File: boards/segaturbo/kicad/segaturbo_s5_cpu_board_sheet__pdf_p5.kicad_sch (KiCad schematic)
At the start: 40 parts, among them CN4 Conn_01x06, CN5 Conn_01x12, CN6 Conn_01x06, CN8 Conn_01x46, IC125 74LS259, IC126 75468, IC127 74LS244, IC17 74LS191, IC35b 74LS74, IC5 74LS191, IC6 8255, IC82 74LS48, IC83 74LS48, IC84 8279, IC95 75468, IC96 75468, IC97 74LS145, IC98 74LS145, SW1 DIP_SW_8, SW2 DIP_SW_8

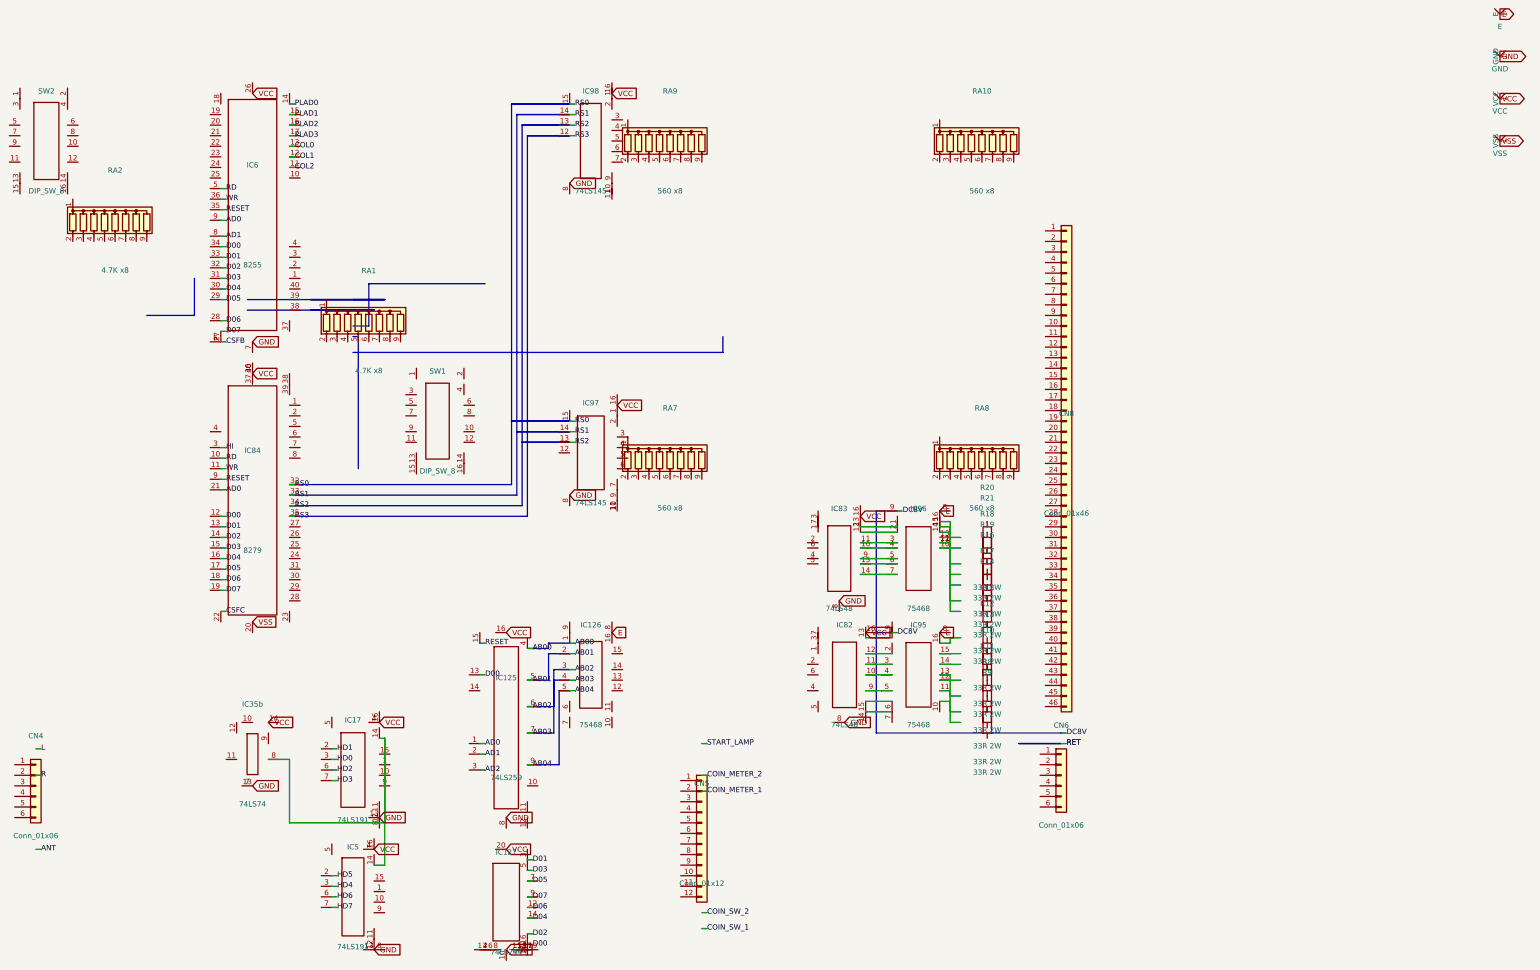
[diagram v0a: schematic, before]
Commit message: Fix KiCad pin-aligned generated symbols
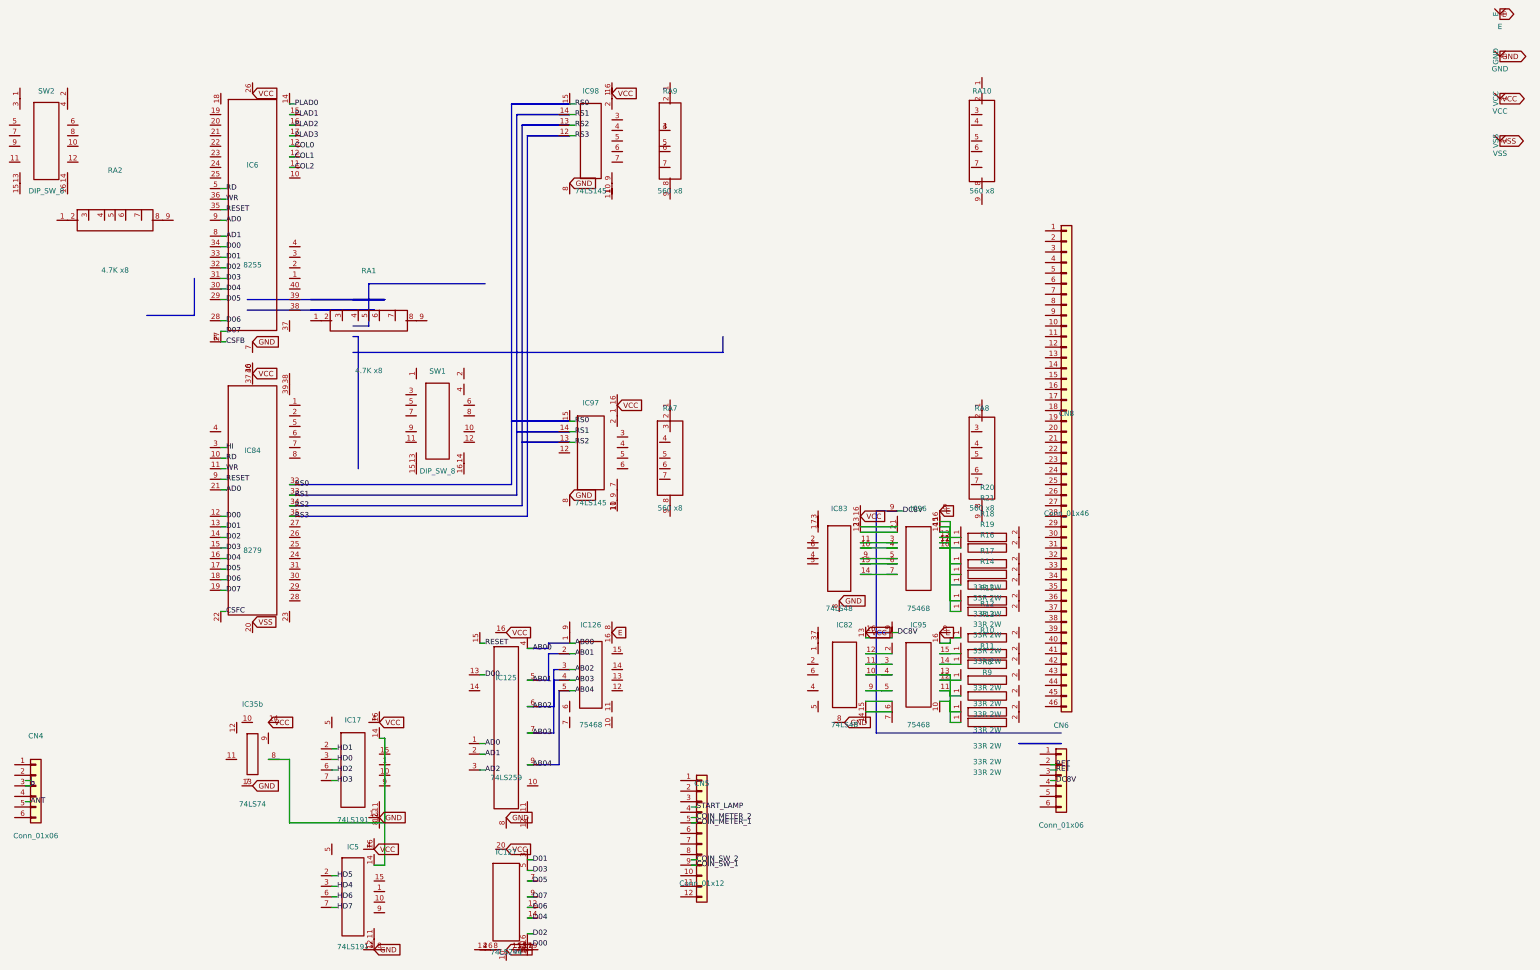
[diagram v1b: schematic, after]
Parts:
- R10: symbol Device:R -> user:_chip_R10
- R11: symbol Device:R -> user:_chip_R11
- R12: symbol Device:R -> user:_chip_R12
- R13: symbol Device:R -> user:_chip_R13
- R14: symbol Device:R -> user:_chip_R14
- R15: symbol Device:R -> user:_chip_R15
- R16: symbol Device:R -> user:_chip_R16
- R17: symbol Device:R -> user:_chip_R17
- R18: symbol Device:R -> user:_chip_R18
- R19: symbol Device:R -> user:_chip_R19
- R20: symbol Device:R -> user:_chip_R20
- R21: symbol Device:R -> user:_chip_R21
- R8: symbol Device:R -> user:_chip_R8
- R9: symbol Device:R -> user:_chip_R9
- RA1: symbol Device:R_Network08 -> user:_chip_RA1
- RA10: symbol Device:R_Network08 -> user:_chip_RA10
- RA2: symbol Device:R_Network08 -> user:_chip_RA2
- RA7: symbol Device:R_Network08 -> user:_chip_RA7
- RA8: symbol Device:R_Network08 -> user:_chip_RA8
- RA9: symbol Device:R_Network08 -> user:_chip_RA9
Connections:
- net at R19.1: now also IC96.10 (7C), IC96.11 (6C), IC96.12 (5C), IC96.13 (4C), IC96.14 (3C), IC96.15 (2C), IC96.16 (1C), R14.1, R16.1, R17.1, R18.1, R20.1, R21.1
- net at R10.1: now also IC95.10 (7C), IC95.11 (6C), IC95.12 (5C), IC95.13 (4C), R11.1, R8.1, R9.1
- net at R10.2: no longer R8.1
- net at RA9.3: now also RA9.4
- net at R13.2: no longer R11.1
- net at R13.1: now also IC95.14 (3C)
- net at R15.1: now also IC95.16 (1C)
- net at R12.1: now also IC95.15 (2C)
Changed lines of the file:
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@@
   )
   (symbol
-    (lib_id "Device:R_Network08")
+    (lib_id "user:_chip_RA2")
     (at 67.31 67.31 0)
     (unit 1)
@@
   )
   (symbol
-    (lib_id "Device:R_Network08")
+    (lib_id "user:_chip_RA1")
     (at 128.27 91.44 0)
     (unit 1)
@@
   )
   (symbol
-    (lib_id "Device:R_Network08")
+    (lib_id "user:_chip_RA9")
     (at 200.66 48.26 0)
     (unit 1)
@@
   )
   (symbol
-    (lib_id "Device:R_Network08")
+    (lib_id "user:_chip_RA10")
     (at 275.59 48.26 0)
     (unit 1)
@@
   )
   (symbol
-    (lib_id "Device:R_Network08")
+    (lib_id "user:_chip_RA7")
     (at 200.66 124.46 0)
     (unit 1)
@@
   )
   (symbol
-    (lib_id "Device:R_Network08")
+    (lib_id "user:_chip_RA8")
     (at 275.59 124.46 0)
     (unit 1)
@@
   )
   (symbol
-    (lib_id "Device:R")
+    (lib_id "user:_chip_R20")
     (at 276.86 143.51 0)
     (unit 1)
@@
   )
   (symbol
-    (lib_id "Device:R")
+    (lib_id "user:_chip_R21")
     (at 276.86 146.05 0)
     (unit 1)
@@
   )
   (symbol
-    (lib_id "Device:R")
+    (lib_id "user:_chip_R18")
     (at 276.86 149.86 0)
     (unit 1)
@@
   )
   (symbol
-    (lib_id "Device:R")
+    (lib_id "user:_chip_R19")
     (at 276.86 152.4 0)
     (unit 1)
@@
   )
   (symbol
-    (lib_id "Device:R")
+    (lib_id "user:_chip_R16")
     (at 276.86 154.94 0)
     (unit 1)
@@
   )
   (symbol
-    (lib_id "Device:R")
+    (lib_id "user:_chip_R17")
     (at 276.86 158.75 0)
     (unit 1)
@@
   )
   (symbol
-    (lib_id "Device:R")
+    (lib_id "user:_chip_R14")
     (at 276.86 161.29 0)
     (unit 1)
@@
   )
   (symbol
-    (lib_id "Device:R")
+    (lib_id "user:_chip_R15")
     (at 276.86 167.64 0)
     (unit 1)
@@
   )
   (symbol
-    (lib_id "Device:R")
+    (lib_id "user:_chip_R12")
     (at 276.86 171.45 0)
     (unit 1)
@@
   )
   (symbol
-    (lib_id "Device:R")
+    (lib_id "user:_chip_R13")
     (at 276.86 173.99 0)
     (unit 1)
@@
   )
   (symbol
-    (lib_id "Device:R")
+    (lib_id "user:_chip_R10")
     (at 276.86 177.8 0)
     (unit 1)
@@
   )
   (symbol
-    (lib_id "Device:R")
+    (lib_id "user:_chip_R11")
     (at 276.86 181.61 0)
     (unit 1)
@@
   )
   (symbol
-    (lib_id "Device:R")
+    (lib_id "user:_chip_R8")
     (at 276.86 185.42 0)
     (unit 1)
@@
   )
   (symbol
-    (lib_id "Device:R")
+    (lib_id "user:_chip_R9")
     (at 276.86 187.96 0)
     (unit 1)
@@
     (stroke (width 0) (type default))
   )
-  (wire (pts (xy 48.26 194.31) (xy 49.53 194.31))
-    (stroke (width 0) (type default))
-  )
-  (wire (pts (xy 48.26 200.66) (xy 49.53 200.66))
-    (stroke (width 0) (type default))
-  )
-  (wire (pts (xy 48.26 218.44) (xy 49.53 218.44))
-    (stroke (width 0) (type default))
-  )
-  (wire (pts (xy 208.28 204.47) (xy 209.55 204.47))
-    (stroke (width 0) (type default))
-  )
-  (wire (pts (xy 208.28 200.66) (xy 209.55 200.66))
-    (stroke (width 0) (type default))
-  )
-  (wire (pts (xy 208.28 193.04) (xy 209.55 193.04))
-    (stroke (width 0) (type default))
-  )
-  (wire (pts (xy 208.28 237.49) (xy 209.55 237.49))
-    (stroke (width 0) (type default))
-  )
-  (wire (pts (xy 208.28 233.68) (xy 209.55 233.68))
-    (stroke (width 0) (type default))
-  )
-  (wire (pts (xy 294.64 190.5) (xy 295.91 190.5))
+  (wire (pts (xy 45.72 201.93) (xy 46.99 201.93))
+    (stroke (width 0) (type default))
+  )
+  (wire (pts (xy 45.72 203.2) (xy 46.99 203.2))
+    (stroke (width 0) (type default))
+  )
+  (wire (pts (xy 45.72 207.01) (xy 46.99 207.01))
+    (stroke (width 0) (type default))
+  )
+  (wire (pts (xy 205.74 212.09) (xy 207.01 212.09))
+    (stroke (width 0) (type default))
+  )
+  (wire (pts (xy 205.74 210.82) (xy 207.01 210.82))
+    (stroke (width 0) (type default))
+  )
+  (wire (pts (xy 205.74 208.28) (xy 207.01 208.28))
+    (stroke (width 0) (type default))
+  )
+  (wire (pts (xy 205.74 222.25) (xy 207.01 222.25))
+    (stroke (width 0) (type default))
+  )
+  (wire (pts (xy 205.74 220.98) (xy 207.01 220.98))
+    (stroke (width 0) (type default))
+  )
+  (wire (pts (xy 292.1 201.93) (xy 293.37 201.93))
     (stroke (width 0) (type default))
   )
@@
     (stroke (width 0) (type default))
   )
-  (wire (pts (xy 294.64 193.04) (xy 295.91 193.04))
+  (wire (pts (xy 292.1 198.12) (xy 293.37 198.12))
+    (stroke (width 0) (type default))
+  )
+  (wire (pts (xy 292.1 199.39) (xy 293.37 199.39))
     (stroke (width 0) (type default))
   )
@@
     (effects (font (size 1.27 1.27)) (justify left))
   )
-  (label "L" (at 49.53 194.31 0)
-    (effects (font (size 1.27 1.27)) (justify left))
-  )
-  (label "R" (at 49.53 200.66 0)
-    (effects (font (size 1.27 1.27)) (justify left))
-  )
-  (label "ANT" (at 49.53 218.44 0)
-    (effects (font (size 1.27 1.27)) (justify left))
-  )
-  (label "COIN_METER_1" (at 209.55 204.47 0)
-    (effects (font (size 1.27 1.27)) (justify left))
-  )
-  (label "COIN_METER_2" (at 209.55 200.66 0)
-    (effects (font (size 1.27 1.27)) (justify left))
-  )
-  (label "START_LAMP" (at 209.55 193.04 0)
-    (effects (font (size 1.27 1.27)) (justify left))
-  )
-  (label "COIN_SW_1" (at 209.55 237.49 0)
-    (effects (font (size 1.27 1.27)) (justify left))
-  )
-  (label "COIN_SW_2" (at 209.55 233.68 0)
-    (effects (font (size 1.27 1.27)) (justify left))
-  )
-  (label "DC8V" (at 295.91 190.5 0)
+  (label "L" (at 46.99 201.93 0)
+    (effects (font (size 1.27 1.27)) (justify left))
+  )
+  (label "R" (at 46.99 203.2 0)
+    (effects (font (size 1.27 1.27)) (justify left))
+  )
+  (label "ANT" (at 46.99 207.01 0)
+    (effects (font (size 1.27 1.27)) (justify left))
+  )
+  (label "COIN_METER_1" (at 207.01 212.09 0)
+    (effects (font (size 1.27 1.27)) (justify left))
+  )
+  (label "COIN_METER_2" (at 207.01 210.82 0)
+    (effects (font (size 1.27 1.27)) (justify left))
+  )
+  (label "START_LAMP" (at 207.01 208.28 0)
+    (effects (font (size 1.27 1.27)) (justify left))
+  )
+  (label "COIN_SW_1" (at 207.01 222.25 0)
+    (effects (font (size 1.27 1.27)) (justify left))
+  )
+  (label "COIN_SW_2" (at 207.01 220.98 0)
+    (effects (font (size 1.27 1.27)) (justify left))
+  )
+  (label "DC8V" (at 293.37 201.93 0)
     (effects (font (size 1.27 1.27)) (justify left))
   )
@@
     (effects (font (size 1.27 1.27)) (justify left))
   )
-  (label "RET" (at 295.91 193.04 0)
-    (effects (font (size 1.27 1.27)) (justify left))
-  )
-  (label "RET" (at 295.91 193.04 0)
-    (effects (font (size 1.27 1.27)) (justify left))
-  )
+  (label "RET" (at 293.37 198.12 0)
+    (effects (font (size 1.27 1.27)) (justify left))
+  )
+  (label "RET" (at 293.37 199.39 0)
+    (effects (font (size 1.27 1.27)) (justify left))
+  )
